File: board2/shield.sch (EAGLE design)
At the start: 41 parts, among them IC1 LM75, J3 22-05-7028-02, J4 WEALTHMETAL DS-214B, J5 22-05-7038-03, K1 G5L, Q1 BC817, U1 LM2596S-5.0

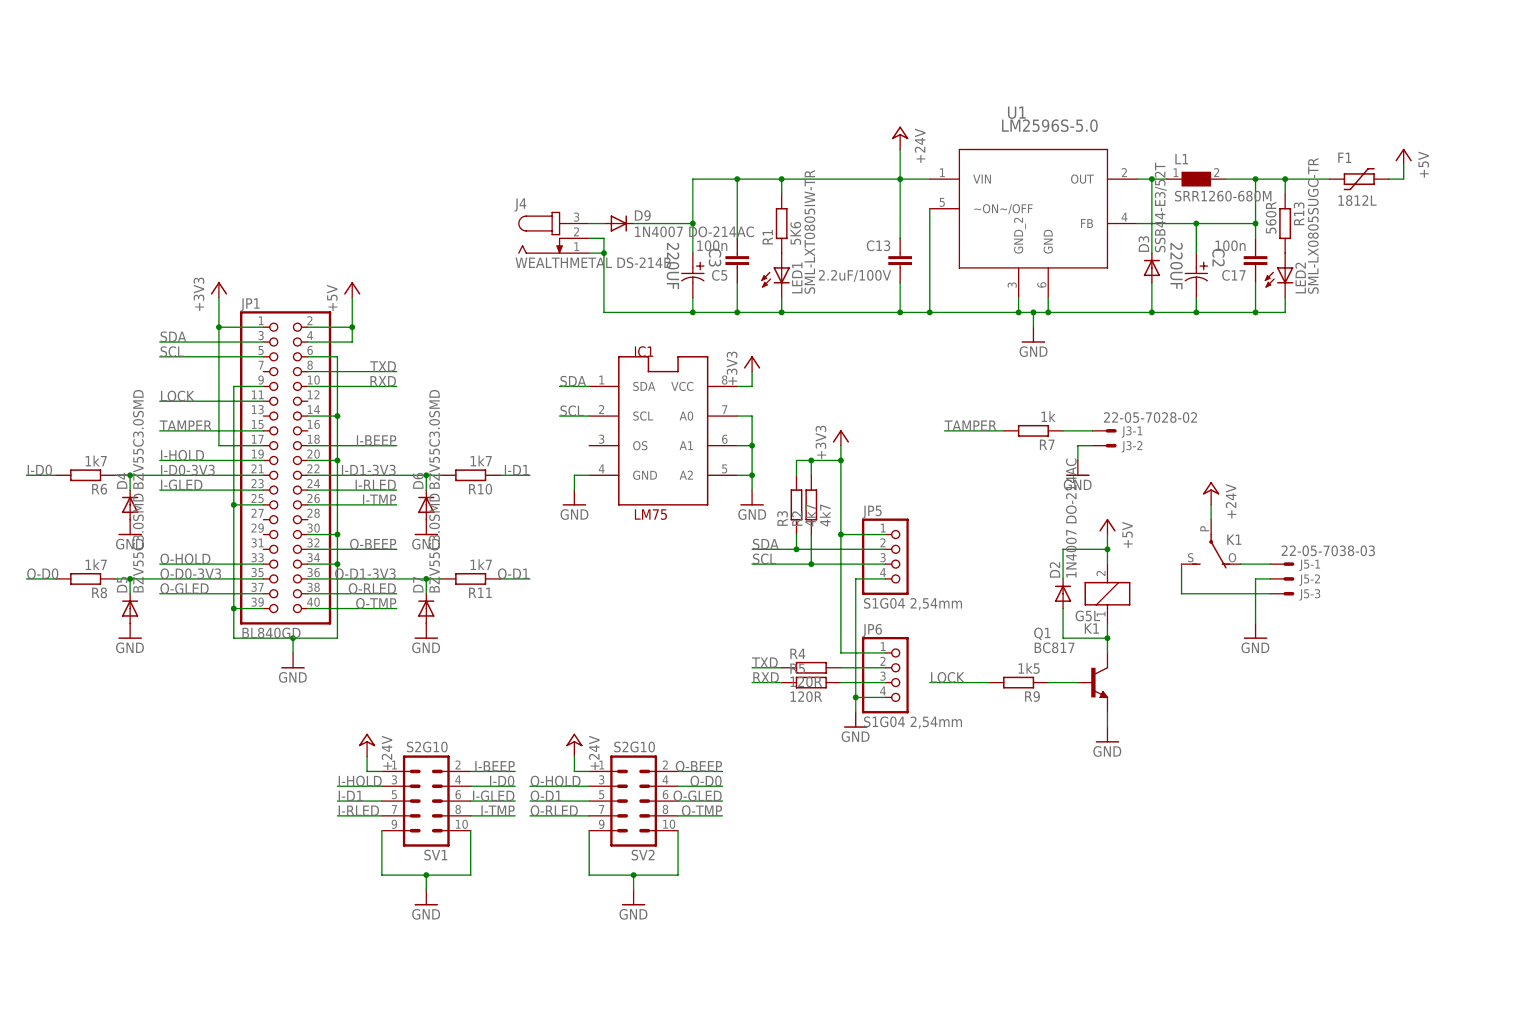
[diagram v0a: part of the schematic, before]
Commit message: Led added, parts renumbered
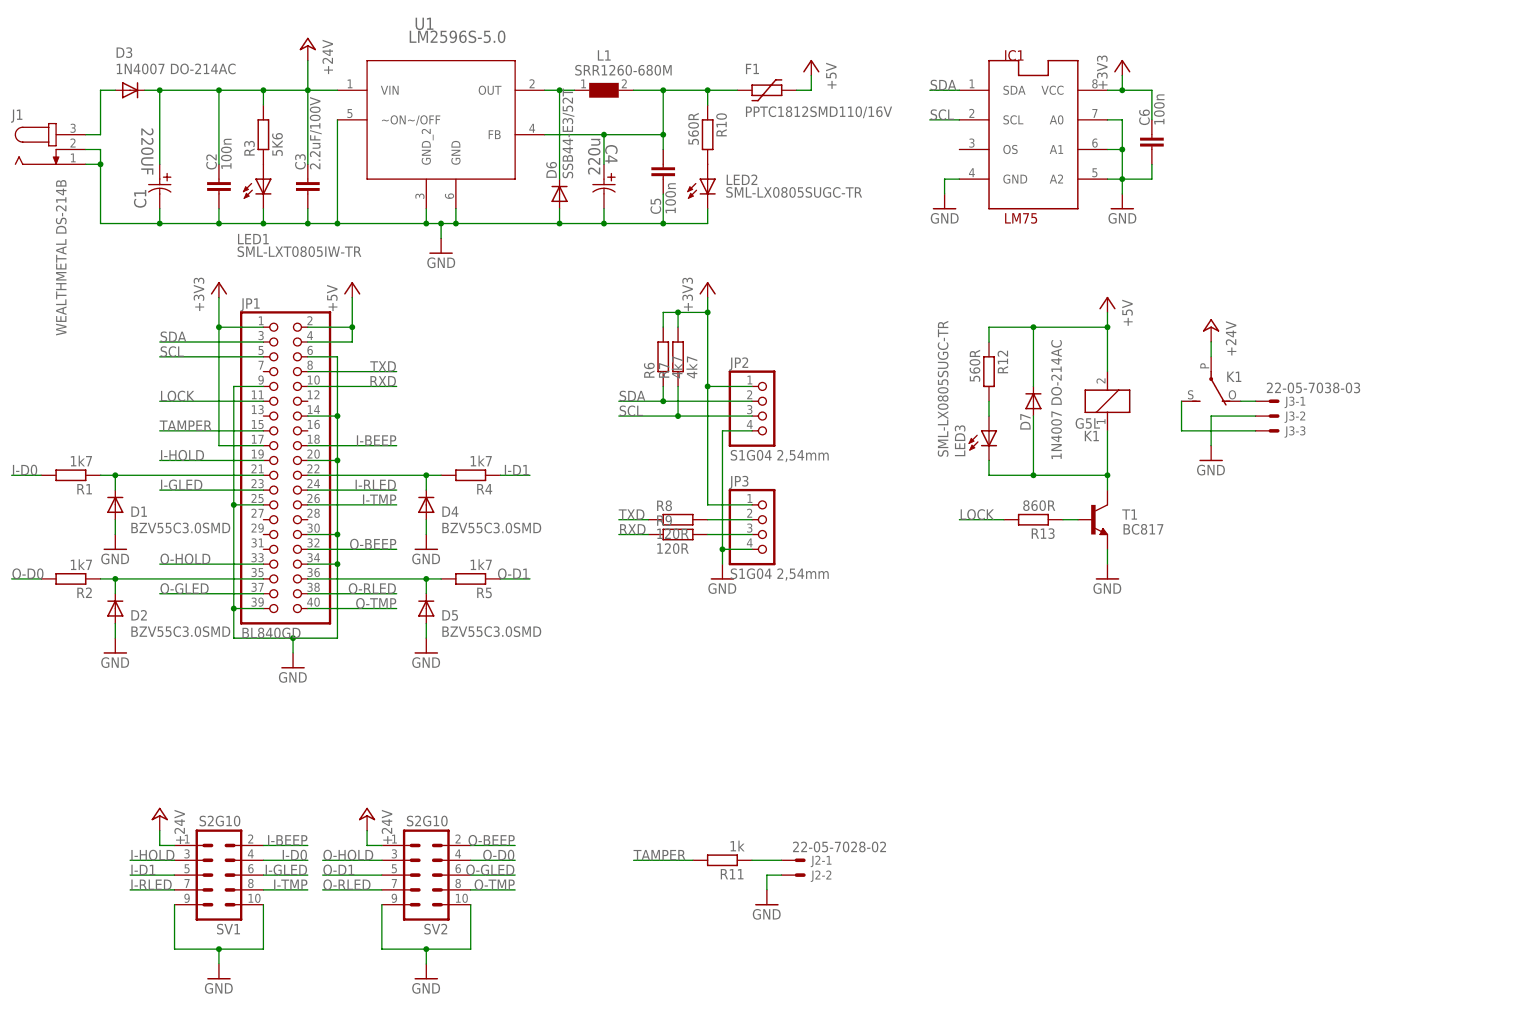
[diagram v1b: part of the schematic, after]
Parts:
- removed C13: 2.2uF/100V, rcl:C-EUC1206
- removed C17: 100n, rcl:C-EUC0805
- removed D9: 1N4007 DO-214AC, diode:DIODE-DO-214AC
- removed J4: WEALTHMETAL DS-214B, con-jack:JACK-PLUG0
- removed J5: 22-05-7038-03, con-molex:22-05-7038-03
- removed JP5, JP6: S1G04 2,54mm, pinhead:PINHD-1X4
- removed Q1: BC817, transistor:BC817-16-NPN-SOT23-BEC
- added C1: 220UF, Panasonic-EEEFK_EEEFP:EEE-FP1V221AP-CASE-F
- added C4: 220u, Panasonic-EEEFK_EEEFP:EEE-FP1V221AP-CASE-F
- added C6: 100n, rcl:C-EUC0805
- added D1: BZV55C3.0SMD, diode:DIODE-MINIMELF
- added J1: WEALTHMETAL DS-214B, con-jack:JACK-PLUG0
- added J2: 22-05-7028-02, con-molex:22-05-7028-02
- added JP2, JP3: S1G04 2,54mm, pinhead:PINHD-1X4
- added LED3: SML-LX0805SUGC-TR, led:LEDCHIPLED_0805
- added R12: 560R, rcl:R-EU_R0805
- added T1: BC817, transistor:BC817-16-NPN-SOT23-BEC
- C2: value 220UF -> 100n; device Panasonic-EEEFK_EEEFP:EEE-FP1V221AP-CASE-F -> rcl:C-EUC0805
- C3: value 220UF -> 2.2uF/100V; device Panasonic-EEEFK_EEEFP:EEE-FP1V221AP-CASE-F -> rcl:C-EUC1206
- D2: value 1N4007 DO-214AC -> BZV55C3.0SMD; device diode:DIODE-DO-214AC -> diode:DIODE-MINIMELF
- D3: value SSB44-E3/52T -> 1N4007 DO-214AC; device diode:DIODE-DO214AA -> diode:DIODE-DO-214AC
- D6: value BZV55C3.0SMD -> SSB44-E3/52T; device diode:DIODE-MINIMELF -> diode:DIODE-DO214AA
- D7: value BZV55C3.0SMD -> 1N4007 DO-214AC; device diode:DIODE-MINIMELF -> diode:DIODE-DO-214AC
- F1: value 1812L -> PPTC1812SMD110/16V
- J3: value 22-05-7028-02 -> 22-05-7038-03; device con-molex:22-05-7028-02 -> con-molex:22-05-7038-03
- R1: value 5K6 -> 1k7
- R10: value 1k7 -> 560R
- R11: value 1k7 -> 1k
- R13: value 560R -> 860R
- R2: value 4k7 -> 1k7
- R3: value 4k7 -> 5K6
- R4, R5: value 120R -> 1k7
- R6: value 1k7 -> 4k7
- R7: value 1k -> 4k7
- R8: value 1k7 -> 120R
- R9: value 1k5 -> 120R
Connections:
- removed net N$9: D9.A, J4.3
- new net N$11: LED3.A, R12.2
- new net UIN: D3.A, J1.3
- net +24V: now also C1.1, C2.2, D3.C, R3.2; no longer C13.1, C5.2, D9.C, R1.2
- net +3V3: now also C6.2, JP2.1, JP3.1, R6.2, R7.2; no longer JP5.1, JP6.1, R2.2, R3.2
- net +5V: now also D7.C, R12.1; no longer D2.C
- net GND: now also C1.2, C2.1, C4.2, C6.1, D1.A, D2.A, J1.1, J1.2, J2-2.S, JP2.4, JP3.4, T1.E; no longer C13.2, C17.1, C2.2, D3.A, D7.A, J4.1, J4.2, J5-2.S, JP5.4, JP6.4, Q1.E
- net I-D0: now also R1.2; no longer R6.2
- net I-D0-3V3: now also D1.C, R1.1; no longer D4.C, R6.1
- net I-D1: now also R4.1; no longer R10.1
- net I-D1-3V3: now also D4.C, R4.2; no longer D6.C, R10.2
- net LOCK: now also R13.2; no longer R9.2
- net N$1: now also C4.1, C5.2, R10.1; no longer C17.2, C2.1, R13.1
- net N$10: now also R13.1, T1.B; no longer Q1.B, R9.1
- net N$2: now also J2-1.S, R11.1; no longer J3-1.S, R7.1
- net N$23: now also R3.1; no longer R1.1
- net N$3: now also JP3.2, R8.2; no longer JP6.2, R4.2
- net N$31: now also D6.C; no longer D3.C
- net N$4: now also R10.2; no longer R13.2
- net N$5: now also J3-3.S; no longer J5-3.S
- net N$6: now also JP3.3, R9.2; no longer JP6.3, R5.2
- net N$7: now also J3-1.S; no longer J5-1.S
- net N$8: now also D7.A, LED3.C, T1.C; no longer D2.A, Q1.C
- net O-D0: now also R2.2; no longer R8.2
- net O-D0-3V3: now also D2.C, R2.1; no longer D5.C, R8.1
- net O-D1: now also R5.1; no longer R11.1
- net O-D1-3V3: now also D5.C, R5.2; no longer D7.C, R11.2
- net RXD: now also R9.1; no longer R5.1
- net SCL: now also JP2.3, R7.1; no longer JP5.3, R2.1
- net SDA: now also JP2.2, R6.1; no longer JP5.2, R3.1
- net TAMPER: now also R11.2; no longer R7.2
- net TXD: now also R8.1; no longer R4.1
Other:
- moved on the sheet: C5, D2, D3, D4, D5, D6, D7, F1, IC1, J3-1, J3-2, K1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
